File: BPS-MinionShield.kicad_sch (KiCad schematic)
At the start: 76 parts, among them J1 TempConn1, J2 TempConn2, J3 Conn_01x24_Female

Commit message: address manthan changes, finalize PR
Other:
- note added: "Version History:"
- note added: "v2.3: Fix footprint issues Update RC values to match timing of the LTC6811 Redo PCB layout to reduce islands and vias v2.2: PCB layout to make everything symmetrical and easier to solder v2.1: Board supports 16 temperature sensors, add RC filter to all temperature sensors"
- note removed: "Change Log: V2.3 Updated PCB routing to reduce GND islands Updated resistor and capacitor values to adjust for LTC startup timing"
- moved on the sheet: H1, H2, H3, H4, PowerLED1, R33

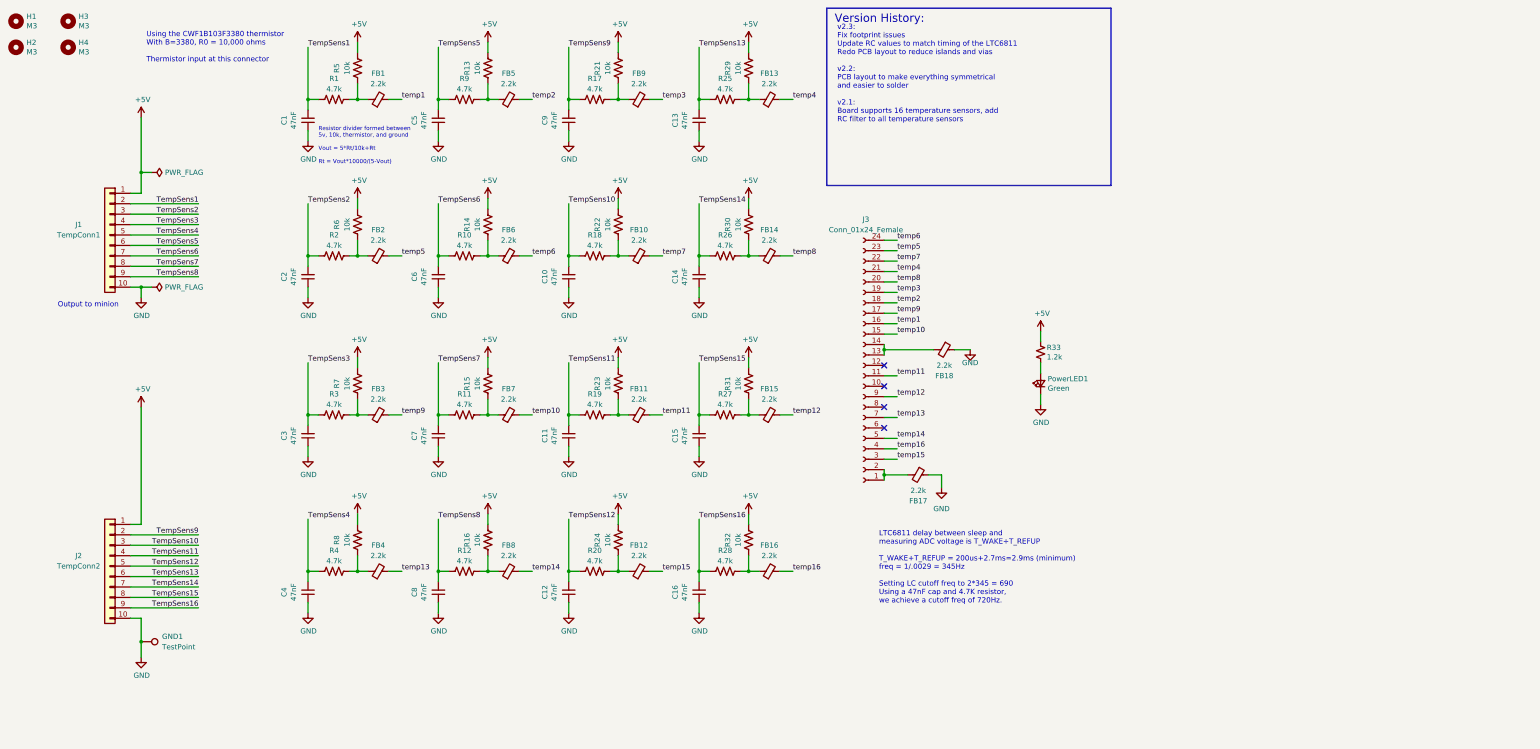
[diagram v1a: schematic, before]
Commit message: started reworking hat
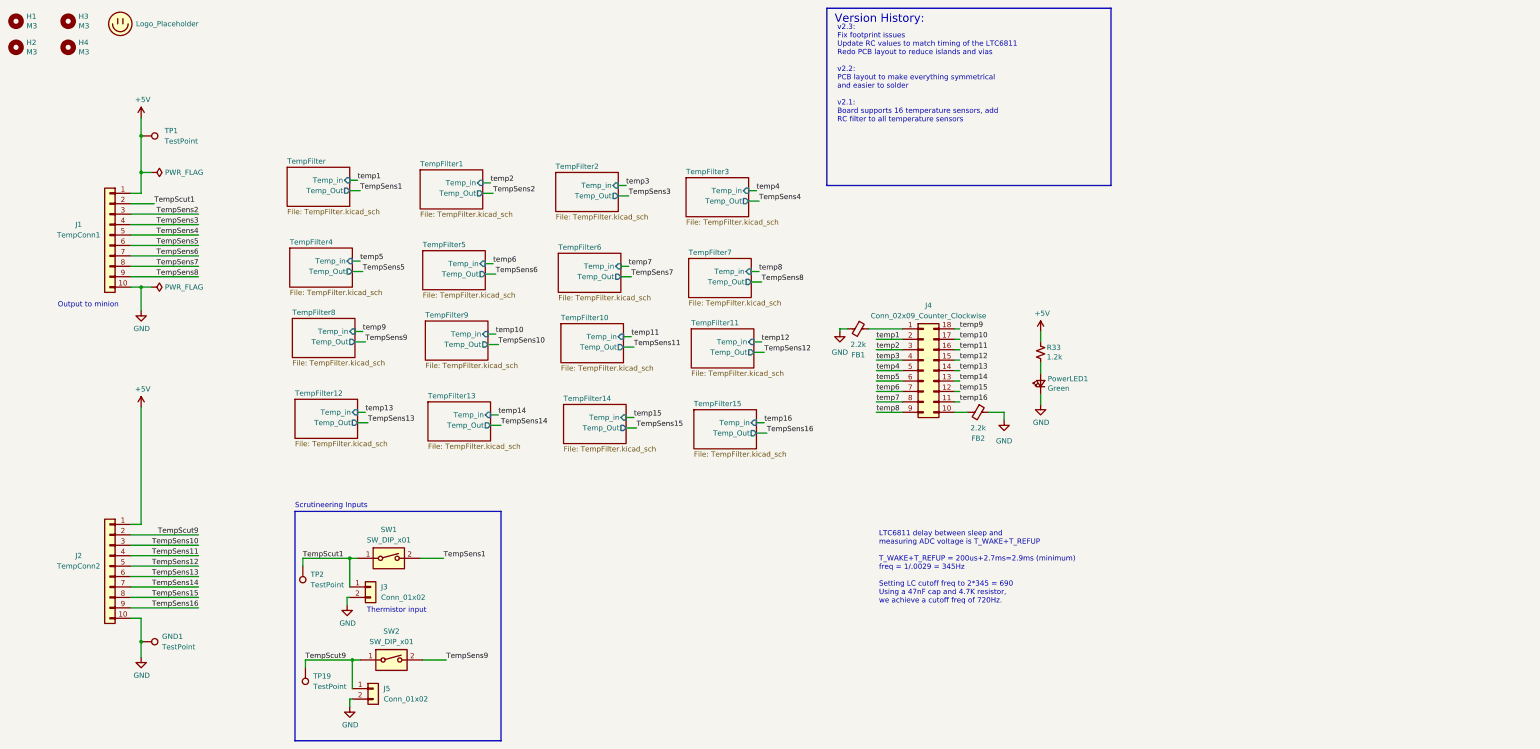
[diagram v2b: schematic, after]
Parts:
- removed C1, C10, C11, C12, C13, C14, C15, C16, C2, C3, C4, C5, C6, C7, C8, C9: 47nF, Capacitor_SMD:C_0805_2012Metric_Pad1.18x1.45mm_HandSolder, symbol Device:C_Small
- removed FB10, FB11, FB12, FB13, FB14, FB15, FB16, FB17, FB18, FB3, FB4, FB5, FB6, FB7, FB8, FB9: 2.2k, Inductor_SMD:L_0805_2012Metric_Pad1.05x1.20mm_HandSolder, symbol Device:FerriteBead_Small
- removed J3: Conn_01x24_Female, UTSVT_Connectors:PADP-24V-1-S, symbol Connector:Conn_01x24_Female
- removed R1, R10, R11, R12, R17, R18, R19, R2, R20, R25, R26, R27, R28, R3, R4, R9: 4.7k, Resistor_SMD:R_0805_2012Metric_Pad1.20x1.40mm_HandSolder, symbol Device:R_US
- removed R13, R14, R15, R16, R21, R22, R23, R24, R29, R30, R31, R32, R5, R6, R7, R8: 10k, Resistor_SMD:R_0805_2012Metric_Pad1.20x1.40mm_HandSolder, symbol Device:R_US
- added J3, J5: Conn_01x02, symbol Connector_Generic:Conn_01x02
- added J4: Conn_02x09_Counter_Clockwise, Connector_Molex:Molex_Micro-Fit_3.0_43045-1800_2x09_P3.00mm_Horizontal, symbol Connector_Generic:Conn_02x09_Counter_Clockwise
- added LOGO1: Logo_Placeholder, UTSVT_Special:Hallock_Image_Small, symbol utsvt-misc:Logo_Placeholder
- added SW1, SW2: SW_DIP_x01, symbol Switch:SW_DIP_x01
- added TP1, TP19, TP2: TestPoint, TestPoint:TestPoint_THTPad_D1.5mm_Drill0.7mm, symbol Connector:TestPoint
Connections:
- net +5V: now also TP1.1
- net GND: now also FB1.2, FB2.1, J3.2 (Pin_2), J5.2 (Pin_2)
- net TempSens1: now also SW1.2; no longer J1.2 (Pin_2)
- net TempSens9: now also SW2.2; no longer J2.2 (Pin_2)
- net temp1: now also J4.2 (Pin_2); no longer FB1.2
- net temp10: now also J4.17 (Pin_17)
- net temp11: now also J4.16 (Pin_16)
- net temp12: now also J4.15 (Pin_15)
- net temp13: now also J4.14 (Pin_14)
- net temp14: now also J4.13 (Pin_13)
- net temp15: now also J4.12 (Pin_12)
- net temp16: now also J4.11 (Pin_11)
- net temp2: now also J4.3 (Pin_3)
- net temp3: now also J4.4 (Pin_4)
- net temp4: now also J4.5 (Pin_5)
- net temp5: now also J4.6 (Pin_6); no longer FB2.2
- net temp6: now also J4.7 (Pin_7)
- net temp7: now also J4.8 (Pin_8)
- net temp8: now also J4.9 (Pin_9)
- net temp9: now also J4.18 (Pin_18)
- net at FB1.1: now also J4.1 (Pin_1)
- new net: FB2.2, J4.10 (Pin_10)
- new net TempScut1: J1.2 (Pin_2), J3.1 (Pin_1), SW1.1, TP2.1
- new net TempScut9: J2.2 (Pin_2), J5.1 (Pin_1), SW2.1, TP19.1
- no-connect marks 4 -> 0
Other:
- added sheet TempFilter (TempFilter.kicad_sch)
- added sheet TempFilter1 (TempFilter.kicad_sch)
- added sheet TempFilter10 (TempFilter.kicad_sch)
- added sheet TempFilter11 (TempFilter.kicad_sch)
- added sheet TempFilter12 (TempFilter.kicad_sch)
- added sheet TempFilter13 (TempFilter.kicad_sch)
- added sheet TempFilter14 (TempFilter.kicad_sch)
- added sheet TempFilter15 (TempFilter.kicad_sch)
- added sheet TempFilter2 (TempFilter.kicad_sch)
- added sheet TempFilter3 (TempFilter.kicad_sch)
- added sheet TempFilter4 (TempFilter.kicad_sch)
- added sheet TempFilter5 (TempFilter.kicad_sch)
- added sheet TempFilter6 (TempFilter.kicad_sch)
- added sheet TempFilter7 (TempFilter.kicad_sch)
- added sheet TempFilter8 (TempFilter.kicad_sch)
- added sheet TempFilter9 (TempFilter.kicad_sch)
- note added: "Scrutineering Inputs"
- note added: "Thermistor input"
- note removed: "Resistor divider formed between 5v, 10k, thermistor, and ground Vout = 5*Rt/10k+Rt Rt = Vout*10000/(5-Vout)"
- note removed: "Using the CWF1B103F3380 thermistor With B=3380, R0 = 10,000 ohms Thermistor input at this connector"

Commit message: fucckkkkk
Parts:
- removed J5: Conn_01x02, symbol Connector_Generic:Conn_01x02
- removed SW1, SW2: SW_DIP_x01, symbol Switch:SW_DIP_x01
- removed TP19: TestPoint, TestPoint:TestPoint_THTPad_D1.5mm_Drill0.7mm, symbol Connector:TestPoint
- added SW?: SW_DIP_x01, MinionShield:DS04254201BKSMT, symbol Switch:SW_DIP_x01
- J3: footprint (none) -> Connector_Molex:Molex_Micro-Fit_3.0_43650-0215_1x02_P3.00mm_Vertical
- J4: p/n (none) -> 43045-1800
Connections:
- net TempScut9 is gone; now on net TempSens9: J2.2 (Pin_2)
- net TempScut1: now also SW?.1
- net TempSens1: now also SW?.2
- net temp1: now also J4.18 (Pin_18); no longer J4.2 (Pin_2)
- net temp10: now also J4.3 (Pin_3); no longer J4.17 (Pin_17)
- net temp11: now also J4.4 (Pin_4); no longer J4.16 (Pin_16)
- net temp12: now also J4.5 (Pin_5); no longer J4.15 (Pin_15)
- net temp13: now also J4.6 (Pin_6); no longer J4.14 (Pin_14)
- net temp14: now also J4.7 (Pin_7); no longer J4.13 (Pin_13)
- net temp15: now also J4.8 (Pin_8); no longer J4.12 (Pin_12)
- net temp16: now also J4.9 (Pin_9); no longer J4.11 (Pin_11)
- net temp2: now also J4.17 (Pin_17); no longer J4.3 (Pin_3)
- net temp3: now also J4.16 (Pin_16); no longer J4.4 (Pin_4)
- net temp4: now also J4.15 (Pin_15); no longer J4.5 (Pin_5)
- net temp5: now also J4.14 (Pin_14); no longer J4.6 (Pin_6)
- net temp6: now also J4.13 (Pin_13); no longer J4.7 (Pin_7)
- net temp7: now also J4.12 (Pin_12); no longer J4.8 (Pin_8)
- net temp8: now also J4.11 (Pin_11); no longer J4.9 (Pin_9)
- net temp9: now also J4.2 (Pin_2); no longer J4.18 (Pin_18)
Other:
- moved on the sheet: FB1

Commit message: board done
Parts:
- FB1, FB2: p/n (none) -> HZ0805B222R-10
- J3: footprint Connector_Molex:Molex_Micro-Fit_3.0_43650-0215_1x02_P3.00mm_Vertical -> UTSVT_Connectors:Molex_MicroFit3.0_1x2xP3.00mm_PolarizingPeg_Vertical; p/n (none) -> 436500227
- PowerLED1: p/n (none) -> 150080VS75000
- R33: p/n (none) -> RT0805FRE071K2L
- gave numbers to parts that had none: 1
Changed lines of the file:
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@@
+			)
+		)
+		(property "p/n" "RT0805FRE071K2L"
+			(at 267.335 97.155 0)
+			(effects
+				(font
+					(size 1.27 1.27)
+				)
+				(hide yes)
 			)
 		)
@@
 		)
 		(property "Description" ""
+			(at 267.335 104.775 0)
+			(effects
+				(font
+					(size 1.27 1.27)
+				)
+				(hide yes)
+			)
+		)
+		(property "p/n" "150080VS75000"
 			(at 267.335 104.775 0)
 			(effects
@@
 		(dnp no)
 		(fields_autoplaced yes)
-		(property "Reference" "SW?"
+		(property "Reference" "SW1"
 			(at 112.395 160.655 0)
 			(effects
@@
 			(project "BPS-MinionShield"
 				(path "/0e9575a4-1ede-4f13-af58-a4e2eef0ca4e"
-					(reference "SW?")
+					(reference "SW1")
 					(unit 1)
 				)
@@
 		)
 		(property "Description" ""
+			(at 252.095 111.76 0)
+			(effects
+				(font
+					(size 1.27 1.27)
+				)
+				(hide yes)
+			)
+		)
+		(property "p/n" "HZ0805B222R-10 "
 			(at 252.095 111.76 0)
 			(effects
@@
 			)
 		)
-		(property "Footprint" "Connector_Molex:Molex_Micro-Fit_3.0_43650-0215_1x02_P3.00mm_Vertical"
+		(property "Footprint" "UTSVT_Connectors:Molex_MicroFit3.0_1x2xP3.00mm_PolarizingPeg_Vertical"
 			(at 103.505 177.8 0)
 			(effects
@@
 		)
 		(property "Description" "Generic connector, single row, 01x02, script generated (kicad-library-utils/schlib/autogen/connector/)"
+			(at 103.505 177.8 0)
+			(effects
+				(font
+					(size 1.27 1.27)
+				)
+				(hide yes)
+			)
+		)
+		(property "p/n" "436500227"
 			(at 103.505 177.8 0)
 			(effects
@@
 			(at 221.615 91.44 0)
 			(effects
+				(font
+					(size 1.27 1.27)
+				)
+				(hide yes)
+			)
+		)
+		(property "p/n" "HZ0805B222R-10 "
+			(at 221.615 91.44 0)
+			(effects
